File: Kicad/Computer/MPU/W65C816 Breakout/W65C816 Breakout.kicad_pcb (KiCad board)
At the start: 2 copper layers, 26.7 x 90.2 mm, 50 parts, among them IC1 74ALVC164245DGG,11, IC10 SN74LVC1G332DCKRG4, IC11 74LVC2G04GW-Q100H, IC12 SN74LVC1G332DCKRG4, IC13 SN74LVC1G332DCKRG4, IC14 SN74LVC1G332DCKRG4, IC15 74LVC2G32DP,125, IC17 74LVC2G08DP-Q100H, IC18 74LVC2G86DP,125, IC19 74LVC125APW-Q100J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

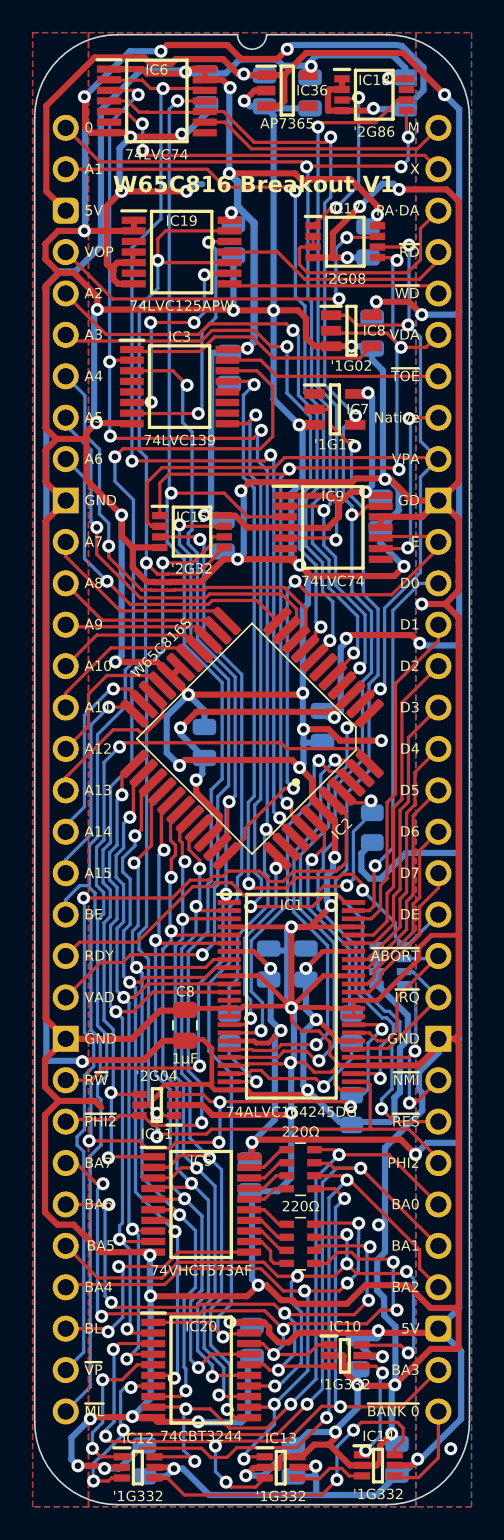
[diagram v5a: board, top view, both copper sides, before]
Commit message: Cleaned up the W65C816 Breakout board and regenerated gerbers.
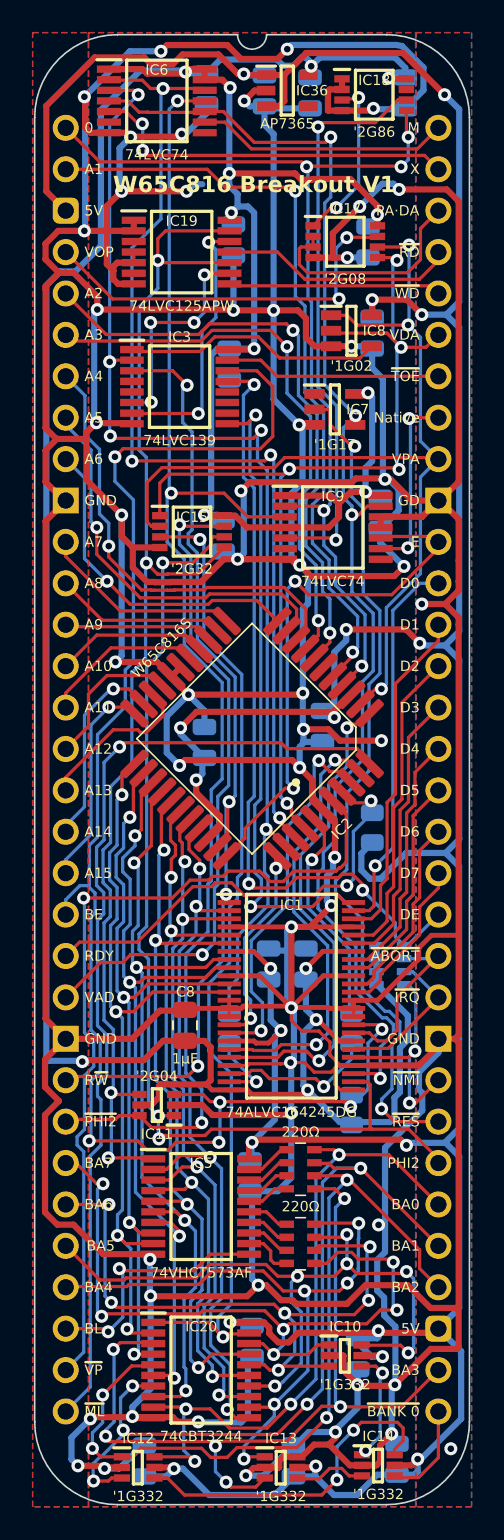
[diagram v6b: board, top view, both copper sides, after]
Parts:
- removed C19: 1μF, SamacSys_Parts:C_0805
- added C23: 1μF, SamacSys_Parts:C_0805, B.Cu at (107.2, 69.0)
- moved C3 0.25 mm to (96.4, 85.6)
- moved IC5 0.13 mm to (94.7, 137.3)
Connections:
- net /W65C816 Breakout Board/3.3V renamed /3.3V
- net /W65C816 Breakout Board/5V renamed /5V
- net /W65C816 Breakout Board/A0 renamed /A0
- net /W65C816 Breakout Board/A0_{CHANGE} renamed /A0_{CHANGE}
- net /W65C816 Breakout Board/A0_{PREV} renamed /A0_{PREV}
- net /W65C816 Breakout Board/A1 renamed /A1
- net /W65C816 Breakout Board/A10 renamed /A10
- net /W65C816 Breakout Board/A11 renamed /A11
- net /W65C816 Breakout Board/A12 renamed /A12
- net /W65C816 Breakout Board/A13 renamed /A13
- net /W65C816 Breakout Board/A14 renamed /A14
- net /W65C816 Breakout Board/A15 renamed /A15
- net /W65C816 Breakout Board/A2 renamed /A2
- net /W65C816 Breakout Board/A3 renamed /A3
- net /W65C816 Breakout Board/A4 renamed /A4
- net /W65C816 Breakout Board/A5 renamed /A5
- net /W65C816 Breakout Board/A6 renamed /A6
- net /W65C816 Breakout Board/A7 renamed /A7
- net /W65C816 Breakout Board/A8 renamed /A8
- net /W65C816 Breakout Board/A9 renamed /A9
- net /W65C816 Breakout Board/Address Valid renamed /Address Valid
- net /W65C816 Breakout Board/BA0 renamed /BA0
- net /W65C816 Breakout Board/BA0+BA1+BA2 renamed /BA0+BA1+BA2
- net /W65C816 Breakout Board/BA1 renamed /BA1
- net /W65C816 Breakout Board/BA2 renamed /BA2
- net /W65C816 Breakout Board/BA3 renamed /BA3
- net /W65C816 Breakout Board/BA3+BA4 renamed /BA3+BA4
- net /W65C816 Breakout Board/BA4 renamed /BA4
- net /W65C816 Breakout Board/BA5 renamed /BA5
- net /W65C816 Breakout Board/BA5+BA6+BA7 renamed /BA5+BA6+BA7
- net /W65C816 Breakout Board/BA6 renamed /BA6
- net /W65C816 Breakout Board/BA7 renamed /BA7
- net /W65C816 Breakout Board/BE renamed /BE
- net /W65C816 Breakout Board/BE_{5V} renamed /BE_{5V}
- net /W65C816 Breakout Board/Bank Latch renamed /Bank Latch
- net /W65C816 Breakout Board/D0 renamed /D0
- net /W65C816 Breakout Board/D0_{65} renamed /D0_{65}
- net /W65C816 Breakout Board/D0_{VHC} renamed /D0_{VHC}
- net /W65C816 Breakout Board/D1 renamed /D1
- net /W65C816 Breakout Board/D1_{65} renamed /D1_{65}
- net /W65C816 Breakout Board/D1_{VHC} renamed /D1_{VHC}
- net /W65C816 Breakout Board/D2 renamed /D2
- net /W65C816 Breakout Board/D2_{65} renamed /D2_{65}
- net /W65C816 Breakout Board/D2_{VHC} renamed /D2_{VHC}
- net /W65C816 Breakout Board/D3 renamed /D3
- net /W65C816 Breakout Board/D3_{65} renamed /D3_{65}
- net /W65C816 Breakout Board/D3_{VHC} renamed /D3_{VHC}
- net /W65C816 Breakout Board/D4 renamed /D4
- net /W65C816 Breakout Board/D4_{65} renamed /D4_{65}
- net /W65C816 Breakout Board/D4_{VHC} renamed /D4_{VHC}
- net /W65C816 Breakout Board/D5 renamed /D5
- net /W65C816 Breakout Board/D5_{65} renamed /D5_{65}
- net /W65C816 Breakout Board/D5_{VHC} renamed /D5_{VHC}
- net /W65C816 Breakout Board/D6 renamed /D6
- net /W65C816 Breakout Board/D6_{65} renamed /D6_{65}
- net /W65C816 Breakout Board/D6_{VHC} renamed /D6_{VHC}
- net /W65C816 Breakout Board/D7 renamed /D7
- net /W65C816 Breakout Board/D7_{65} renamed /D7_{65}
- net /W65C816 Breakout Board/D7_{VHC} renamed /D7_{VHC}
- net /W65C816 Breakout Board/DE renamed /DE
- net /W65C816 Breakout Board/E renamed /E
- net /W65C816 Breakout Board/FET ~{OE} renamed /FET ~{OE}
- net /W65C816 Breakout Board/GND renamed /GND
- net /W65C816 Breakout Board/M renamed /M
- net /W65C816 Breakout Board/MX renamed /MX
- net /W65C816 Breakout Board/Native Latch renamed /Native Latch
- net /W65C816 Breakout Board/Opcode Valid renamed /Opcode Valid
- net /W65C816 Breakout Board/PHI2 renamed /PHI2
- net /W65C816 Breakout Board/PHI2_{5V} renamed /PHI2_{5V}
- net /W65C816 Breakout Board/RDY renamed /RDY
- net /W65C816 Breakout Board/R~{W} renamed /R~{W}
- net /W65C816 Breakout Board/VDA renamed /VDA
- net /W65C816 Breakout Board/VPA renamed /VPA
- net /W65C816 Breakout Board/VPA·VDA renamed /VPA·VDA
- net /W65C816 Breakout Board/X renamed /X
- net /W65C816 Breakout Board/~{ABORT} renamed /~{ABORT}
- net /W65C816 Breakout Board/~{ABORT}_{5V} renamed /~{ABORT}_{5V}
- net /W65C816 Breakout Board/~{BANK 0} renamed /~{BANK 0}
- net /W65C816 Breakout Board/~{BE} renamed /~{BE}
- net /W65C816 Breakout Board/~{DE} renamed /~{DE}
- net /W65C816 Breakout Board/~{IRQ} renamed /~{IRQ}
- net /W65C816 Breakout Board/~{IRQ}_{5V} renamed /~{IRQ}_{5V}
- net /W65C816 Breakout Board/~{ML} renamed /~{ML}
- net /W65C816 Breakout Board/~{NMI} renamed /~{NMI}
- net /W65C816 Breakout Board/~{NMI}_{5V} renamed /~{NMI}_{5V}
- net /W65C816 Breakout Board/~{PHI2} renamed /~{PHI2}
- net /W65C816 Breakout Board/~{RD} renamed /~{RD}
- net /W65C816 Breakout Board/~{RD}_{PART} renamed /~{RD}_{PART}
- net /W65C816 Breakout Board/~{RES}_{5V} renamed /~{RES}_{5V}
- net /W65C816 Breakout Board/~{Reset Sharp} renamed /~{Reset Sharp}
- net /W65C816 Breakout Board/~{Reset} renamed /~{Reset}
- net /W65C816 Breakout Board/~{Trans Output} renamed /~{Trans Output}
- net /W65C816 Breakout Board/~{VPA+VDA} renamed /~{VPA+VDA}
- net /W65C816 Breakout Board/~{VP} renamed /~{VP}
- net /W65C816 Breakout Board/~{WD} renamed /~{WD}
- net /W65C816 Breakout Board/~{WD}_{PART} renamed /~{WD}_{PART}
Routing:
- net /GND: track 673.7 -> 670.7 mm
- net /3.3V: track 217.9 -> 220.0 mm
- net /A3: track 33.3 -> 34.1 mm
- net /BA2: track 50.2 -> 49.6 mm
- net /D6_{65}: track 46.8 -> 46.2 mm

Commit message: Re-autorouted a bunch of boards.  Or something.  I don't know.
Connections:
- J7 pad 1: /A0 -> /Opcode Valid
- J7 pad 2: /A1 -> /A0
- J7 pad 4: /Opcode Valid -> /A1
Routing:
- net /A1: track 47.2 -> 41.2 mm
- net /GND: track 670.7 -> 669.4 mm
- net /A13: track 9.14 -> 8.33 mm
- net /Opcode Valid: track 23.9 -> 24.7 mm
- net /A0: track 62.0 -> 61.4 mm
- net /3.3V: track 220.0 -> 220.5 mm
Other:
- board text added: "A0"
- board text removed: "0"
